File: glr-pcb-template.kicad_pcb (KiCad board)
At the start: 2 copper layers, 1 part

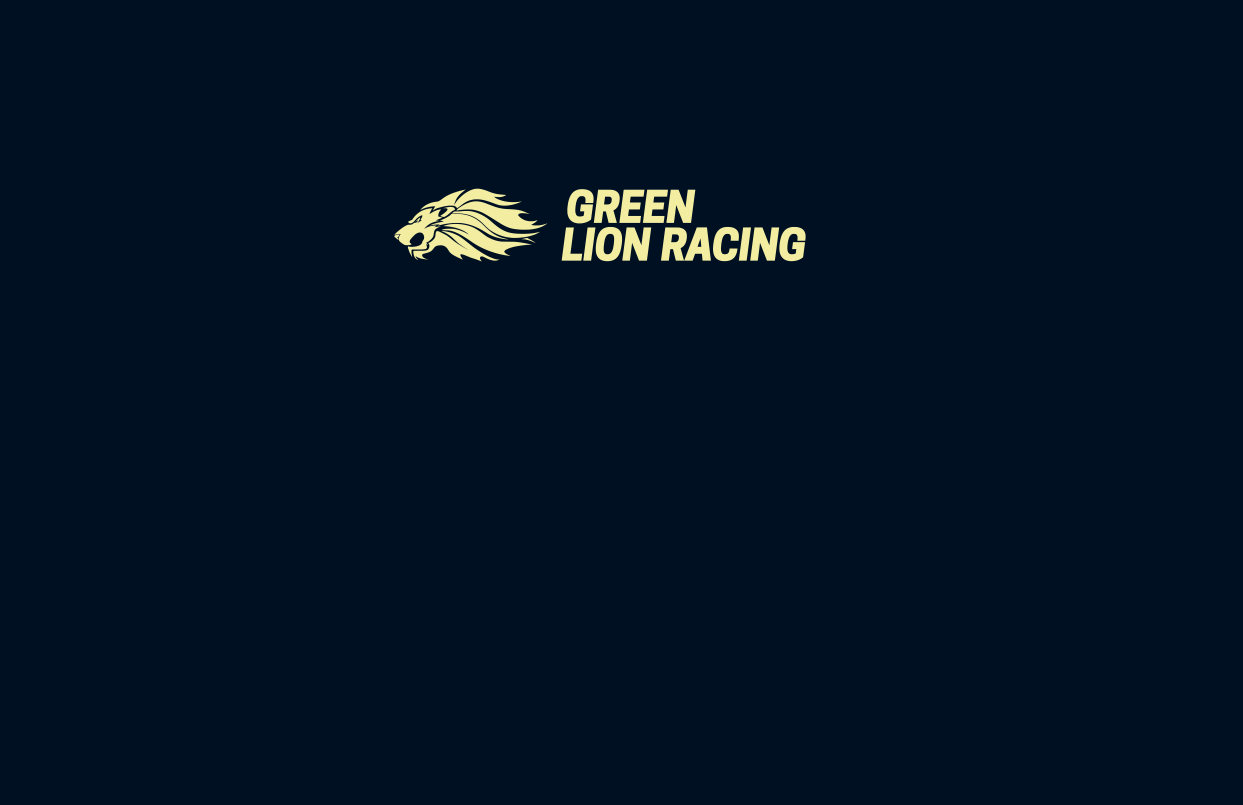
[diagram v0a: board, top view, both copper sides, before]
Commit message: add mounting holes
add simple template board outline
add project overview to pcb silkscreen
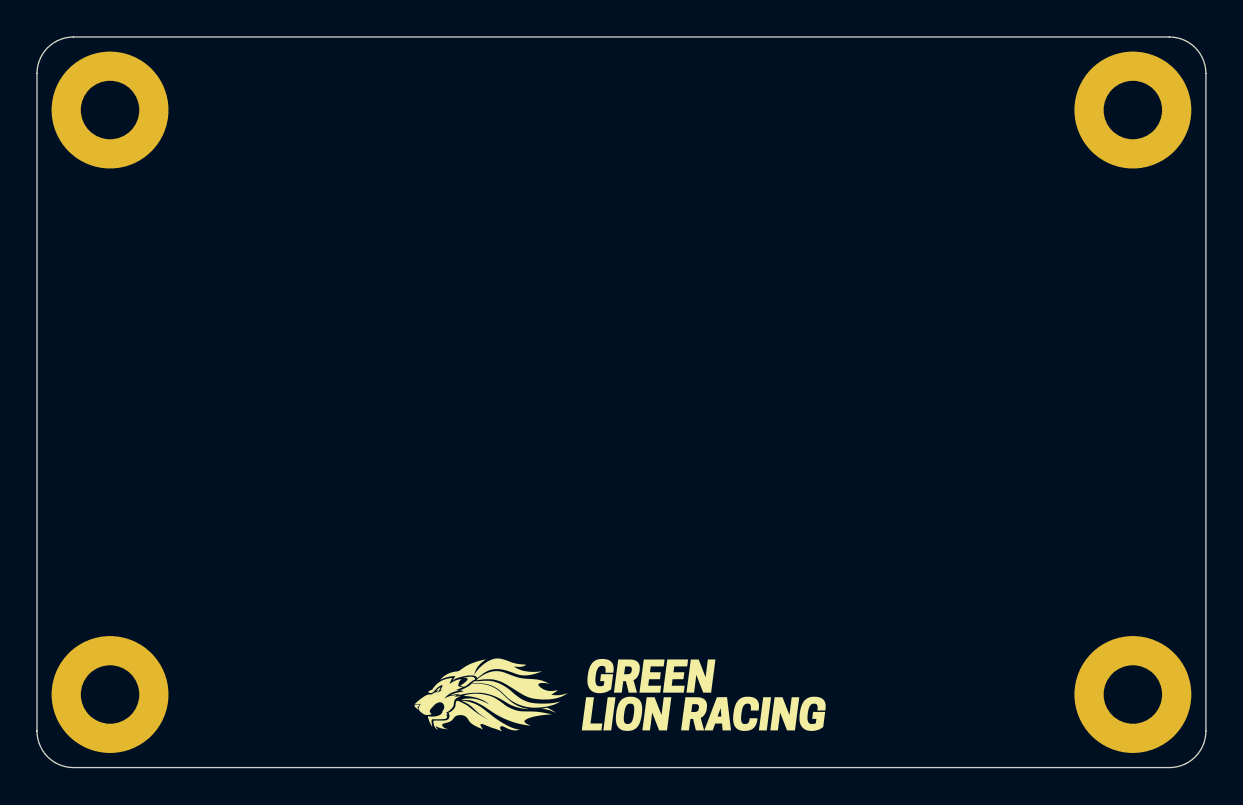
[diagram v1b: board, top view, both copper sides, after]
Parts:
- added REF**: MountingHole_3.2mm_M3_Pad, MountingHole:MountingHole_3.2mm_M3_Pad, F.Cu at (122.0, 94.0)
- added REF**: MountingHole_3.2mm_M3_Pad, MountingHole:MountingHole_3.2mm_M3_Pad, F.Cu at (122.0, 126.0)
- added REF**: MountingHole_3.2mm_M3_Pad, MountingHole:MountingHole_3.2mm_M3_Pad, F.Cu at (178.0, 94.0)
- added REF**: MountingHole_3.2mm_M3_Pad, MountingHole:MountingHole_3.2mm_M3_Pad, F.Cu at (178.0, 126.0)
- moved G*** 25.7 mm to (150.0, 126.0)
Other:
- board outline added: 64 x 40 mm
- copper layers 2 -> 4
- board text added: "${COMPANY} ${TITLE} ${PROJECTNAME} ${REVISION} ${ISSUE_DATE}"
